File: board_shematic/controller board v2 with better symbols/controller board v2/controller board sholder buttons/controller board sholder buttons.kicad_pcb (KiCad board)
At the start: 2 copper layers, 13 x 58 mm, 6 parts, among them J1 Conn_01x03_Pin, J2 Conn_01x03_Pin, SW1 SW_Push, SW2 SW_Push, SW3 SW_Push, SW4 SW_Push

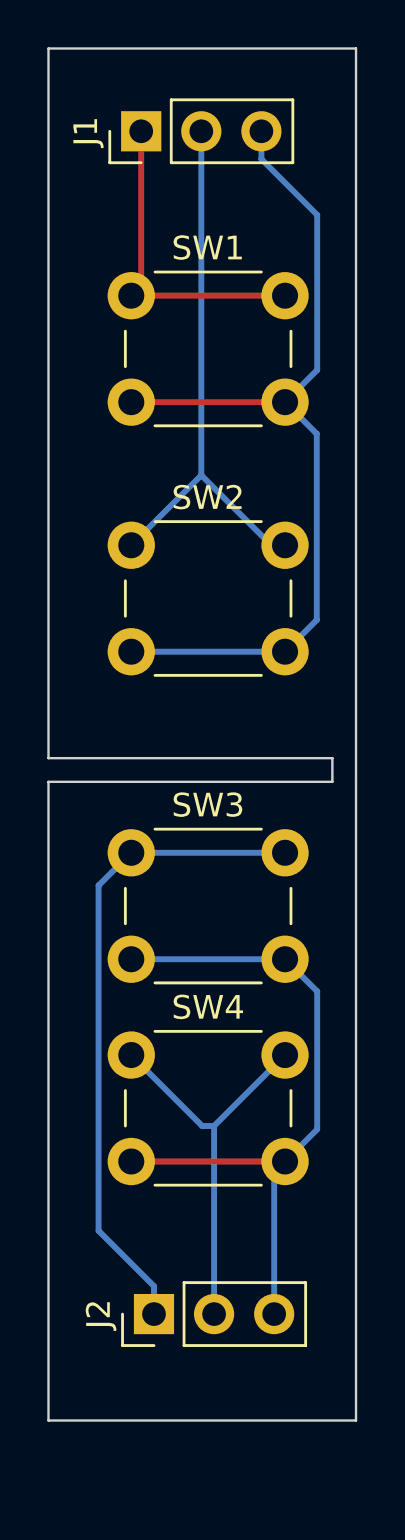
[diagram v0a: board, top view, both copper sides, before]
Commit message: modified sholder buttons
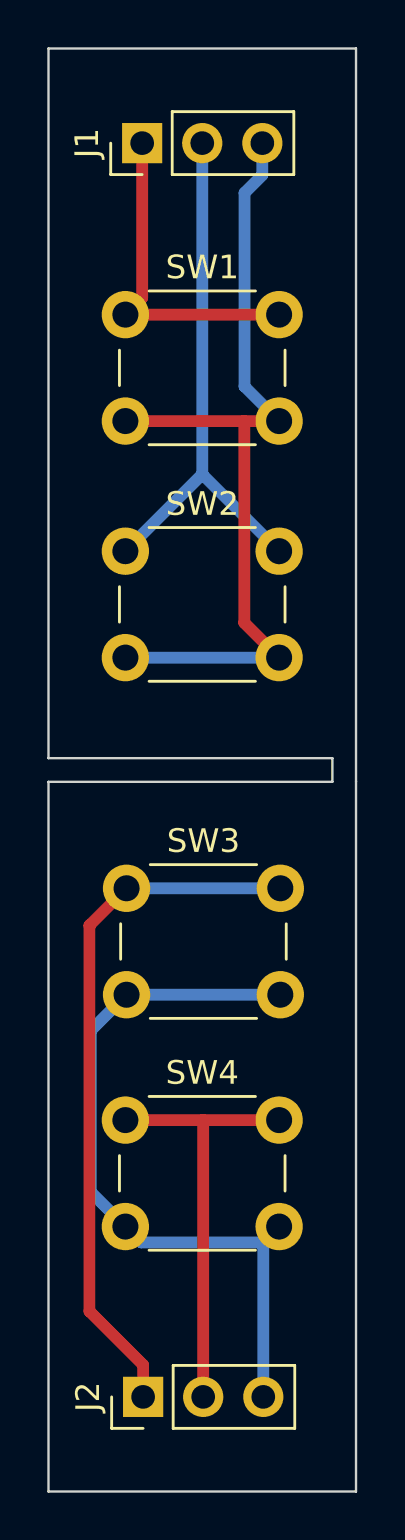
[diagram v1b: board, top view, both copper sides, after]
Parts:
- moved J2 3.53 mm to (158.5, 117.0)
- moved SW4 2.76 mm to (157.8, 105.3)
- moved SW3 1.51 mm to (157.8, 95.5)
- moved SW1 0.84 mm to (157.8, 71.2)
- moved J1 0.50 mm to (158.5, 64.0)
- moved SW2 0.35 mm to (157.8, 81.2)
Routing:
- net Net-(J2-Pin_1): track 27.5 -> 29.6 mm
- net Net-(J2-Pin_3): track 29.3 -> 31.1 mm
- net Net-(J1-Pin_3): track 37.7 -> 36.3 mm
- net Net-(J2-Pin_2): track 16.9 -> 18.2 mm
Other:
- board size 13 x 58 mm -> 13 x 61 mm

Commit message: changed hole locations, updated pin orientation
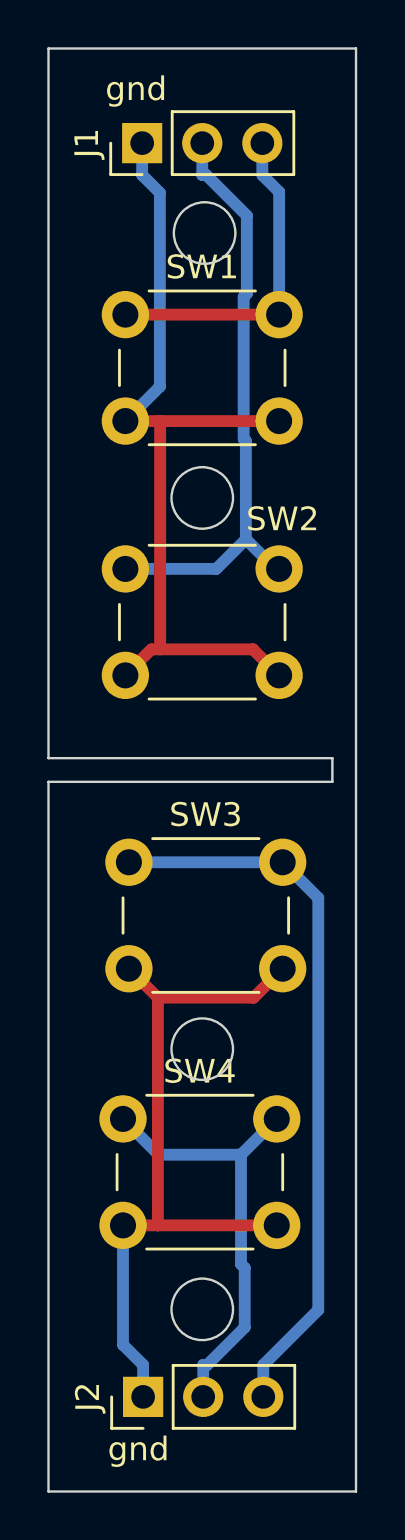
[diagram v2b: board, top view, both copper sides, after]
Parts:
- moved SW3 1.10 mm to (157.9, 94.4)
- moved SW2 0.75 mm to (157.8, 82.0)
- moved SW4 0.11 mm to (157.7, 105.2)
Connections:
- SW1 pad 1: Net-(J1-Pin_1) -> Net-(J1-Pin_3)
- SW1 pad 2: Net-(J1-Pin_3) -> Net-(J1-Pin_1)
- SW2 pad 2: Net-(J1-Pin_3) -> Net-(J1-Pin_1)
- SW3 pad 1: Net-(J2-Pin_1) -> Net-(J2-Pin_3)
- SW3 pad 2: Net-(J2-Pin_3) -> Net-(J2-Pin_1)
- SW4 pad 2: Net-(J2-Pin_3) -> Net-(J2-Pin_1)
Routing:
- net Net-(J1-Pin_3): track 36.3 -> 14.0 mm
- net Net-(J1-Pin_1): track 14.0 -> 36.2 mm
- net Net-(J1-Pin_2): track 23.2 -> 25.3 mm
- net Net-(J2-Pin_1): track 29.6 -> 31.2 mm
- net Net-(J2-Pin_2): track 18.2 -> 18.9 mm
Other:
- outline, holes or cut-outs redrawn
- board text added: "gnd"
